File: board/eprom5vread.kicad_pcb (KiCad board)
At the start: 4 copper layers, 127 x 94 mm, 46 parts, among them J101 DEBUG, J102 UART, J201 Conn_02x21_Counter_Clockwise, J301 Barrel_Jack, SW101 RST, U101 STM32G0B0CETx, U201 MCP23008-E/SS, U202 MCP23008-E/SS, U203 MCP23008-E/SS, U204 MCP23008-E/SS, U205 MCP23008-E/SS, U251 PCA9306DCTR, U252 SN74LV1T34DCK, U301 NCP1117ST33T3G, U302 NCP1117ST50T3G

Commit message: update MCU model name
we use the variant with fewer pins now
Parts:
- U101: value STM32G0B0CETx -> STM32G0B0KETx
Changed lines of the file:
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@@
 			)
 		)
-		(property "Value" "STM32G0B0CETx"
+		(property "Value" "STM32G0B0KETx"
 			(at 0 5.88 0)
 			(layer "F.Fab")

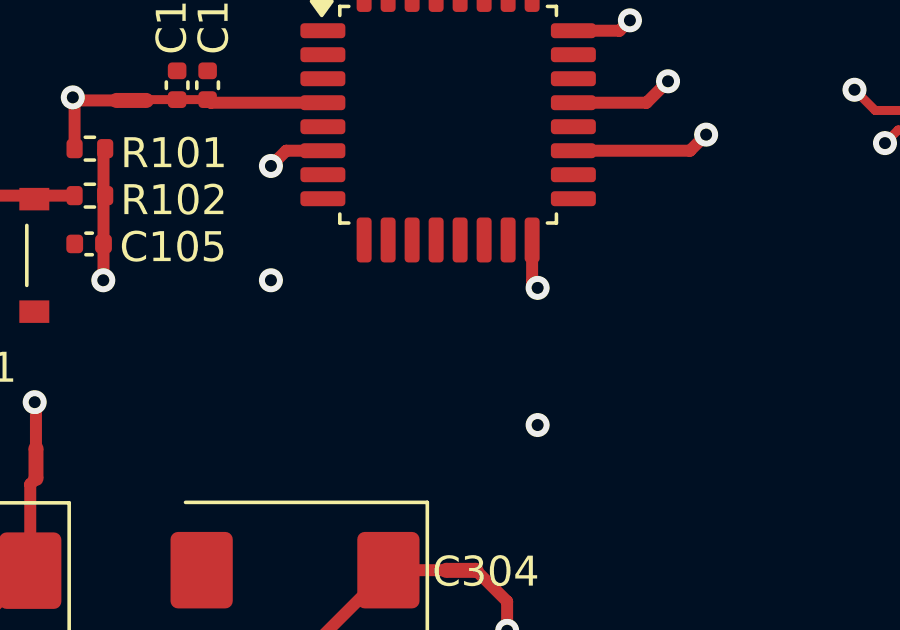
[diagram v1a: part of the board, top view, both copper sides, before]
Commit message: add an LED because everything is better with LEDs
also debugging before UART comes up
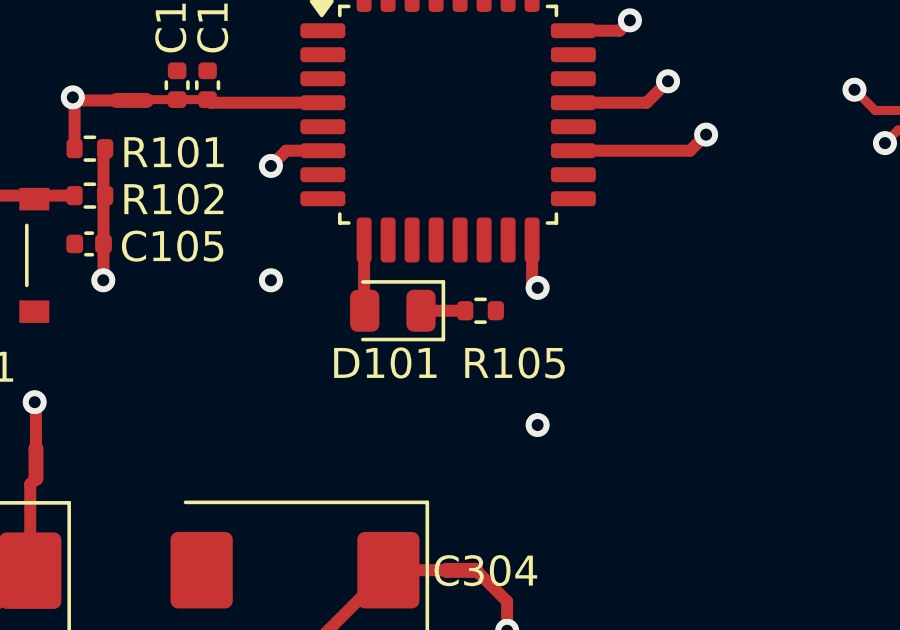
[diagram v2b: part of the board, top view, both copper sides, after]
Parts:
- added D101: LED, LED_SMD:LED_0805_2012Metric, F.Cu at (73.4, 90.4)
- added R105: 22Ω, Resistor_SMD:R_0402_1005Metric, F.Cu at (76.3, 90.4)
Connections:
- U101 pad 9: unconnected-(U101-PA2-Pad9) -> Net-(D101-A)
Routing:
- net Net-(D101-A): track 0.00 -> 2.34 mm
- net Net-(D101-K): track 0.00 -> 1.48 mm
